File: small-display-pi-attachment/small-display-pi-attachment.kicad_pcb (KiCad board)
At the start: 2 copper layers, 56 x 65 mm, 9 parts, among them J1 Conn_01x40, J2 F32D-1A7Y1-21040, J3 Conn_01x03, U2 PAM2804AAB010

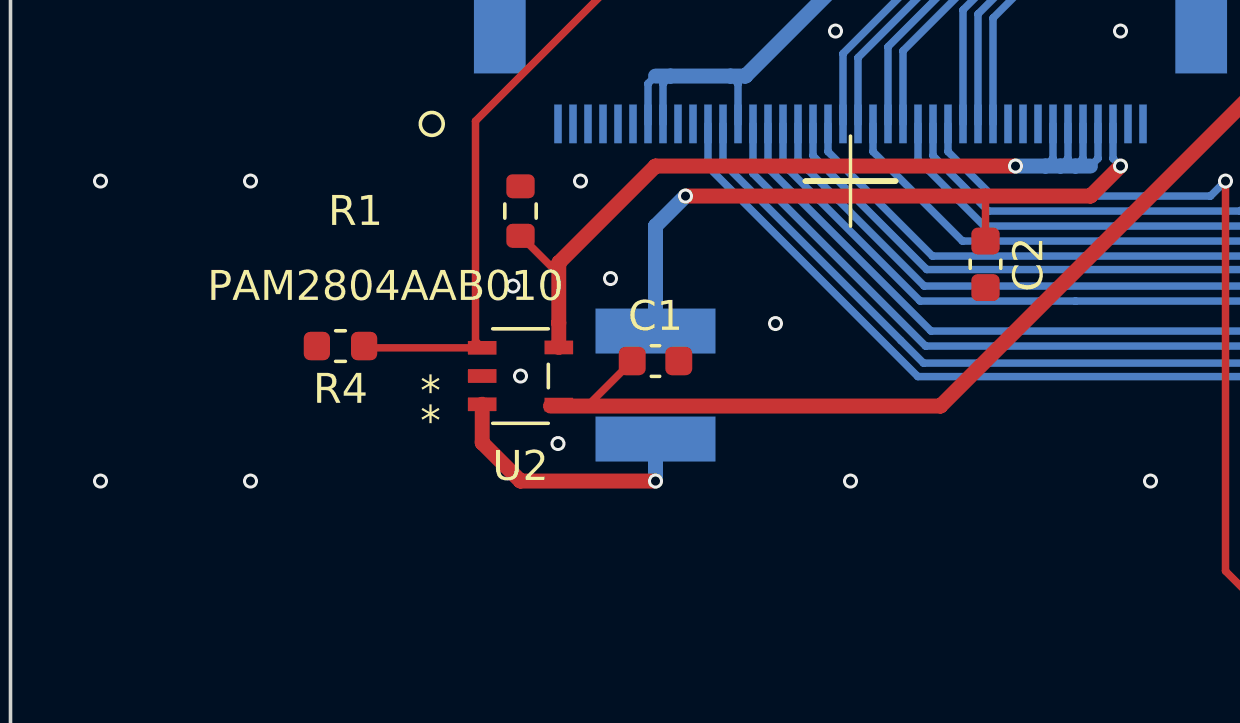
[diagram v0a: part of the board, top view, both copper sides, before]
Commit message: Updated 3D models and silk screen.
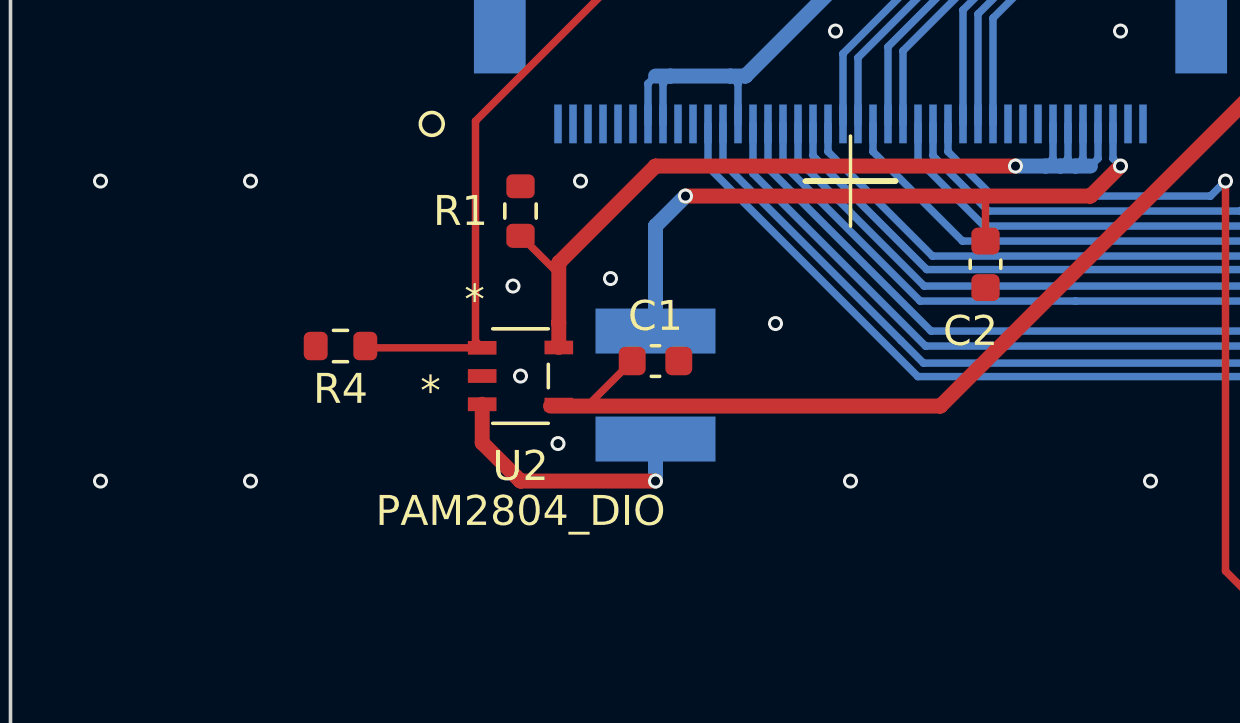
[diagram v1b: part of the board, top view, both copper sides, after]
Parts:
- J2: value F32D-1A7Y1-21040 -> CONN_F32D-1A7Y1-21040_AMP
- U2: value PAM2804AAB010 -> PAM2804_DIO

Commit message: Minor update to clearances.
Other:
- rule pad_to_mask_clearance: 0.051 -> 0
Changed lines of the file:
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@@
       (dielectric_constraints no)
     )
-    (pad_to_mask_clearance 0.051)
-    (solder_mask_min_width 0.25)
+    (pad_to_mask_clearance 0)
     (pcbplotparams
       (layerselection 0x00010fc_ffffffff)
